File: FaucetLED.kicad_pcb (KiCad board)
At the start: 2 copper layers, 34.5 x 25.4 mm, 30 parts, among them P1 CONN_01X03, P2 CONN_01X02, P3 CONN_01X02, P4 CONN_01X03, P5 CONN_01X02, U1 TLV70033DDC, U2 STM32L052KxTx

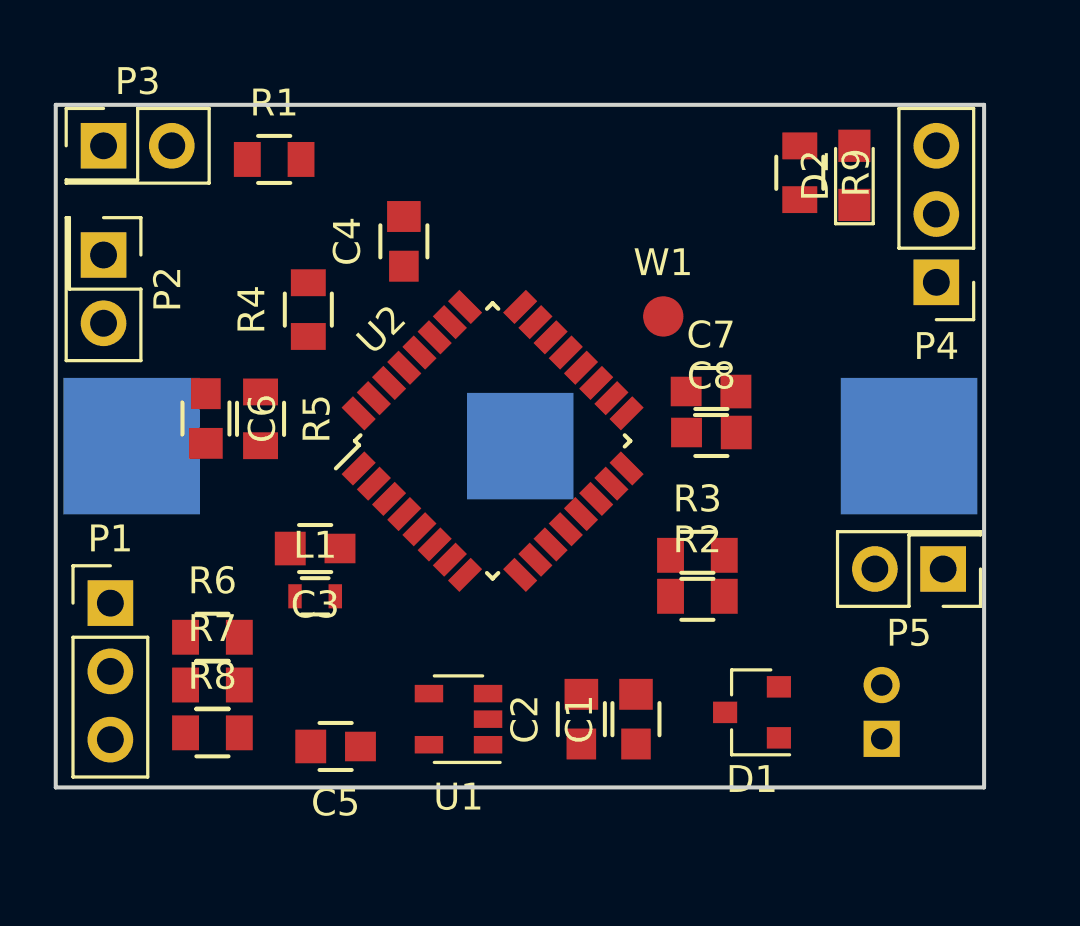
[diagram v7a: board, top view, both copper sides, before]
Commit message: Add mounting holes for CU-18420-B enclosure.
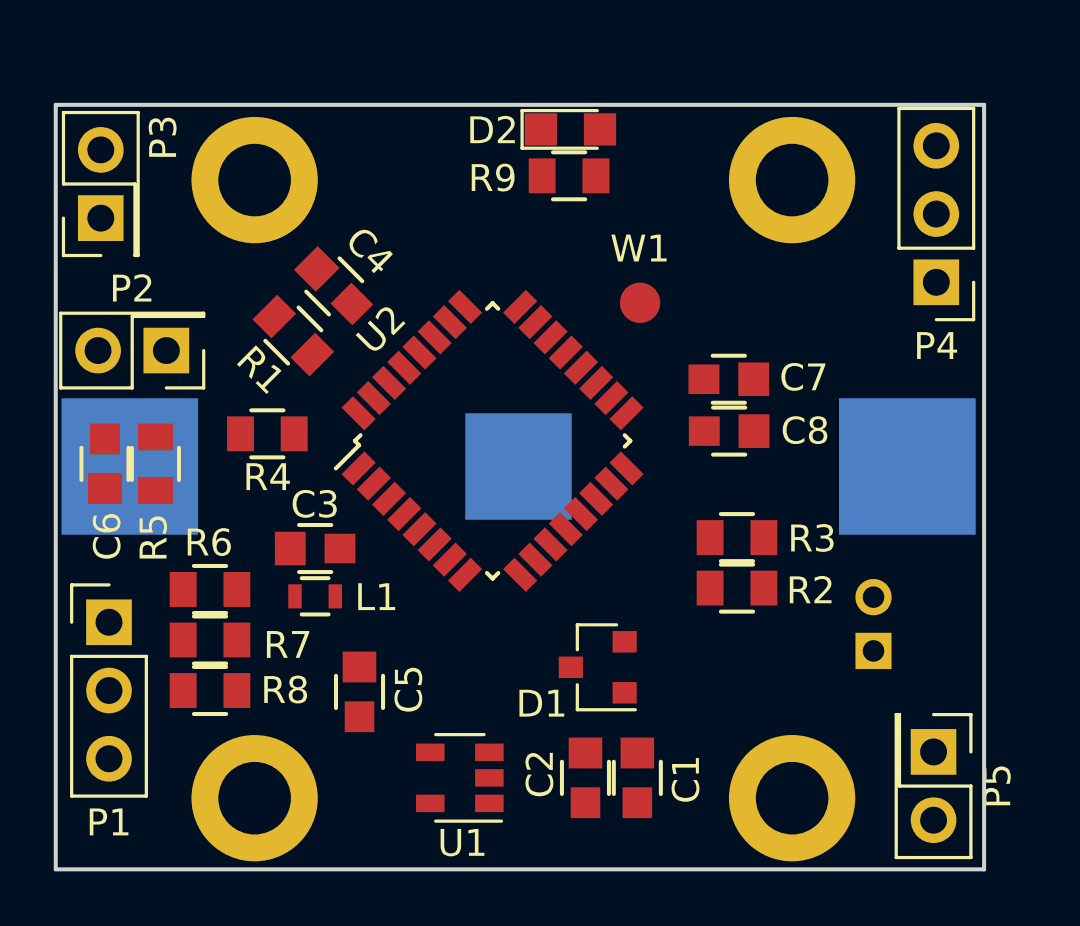
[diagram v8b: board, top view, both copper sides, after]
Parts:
- added REF**: MountingHole_2.7mm_M2.5_DIN965_Pad, Mounting_Holes:MountingHole_2.7mm_M2.5_DIN965_Pad, F.Cu at (109.0, 79.0)
- added REF**: MountingHole_2.7mm_M2.5_DIN965_Pad, Mounting_Holes:MountingHole_2.7mm_M2.5_DIN965_Pad, F.Cu at (129.0, 102.0)
- added REF**: MountingHole_2.7mm_M2.5_DIN965_Pad, Mounting_Holes:MountingHole_2.7mm_M2.5_DIN965_Pad, F.Cu at (129.0, 79.0)
- added REF**: MountingHole_2.7mm_M2.5_DIN965_Pad, Mounting_Holes:MountingHole_2.7mm_M2.5_DIN965_Pad, F.Cu at (109.0, 102.0)
- moved D2 10.7 mm to (120.8, 77.1), turned to 0 degrees
- moved R9 8.59 mm to (120.7, 78.8), turned to 180 degrees
- moved P5 6.82 mm to (134.3, 100.3), turned to 270 degrees
- moved R1 6.59 mm to (110.4, 84.8), turned to 315 degrees
- moved D1 5.98 mm to (121.8, 97.1)
- moved R4 4.87 mm to (109.5, 88.4), turned to 180 degrees
- moved R5 4.26 mm to (105.3, 89.6)
- moved P2 4.26 mm to (105.7, 85.3), turned to 180 degrees
- moved C6 4.12 mm to (103.4, 89.6)
- moved BT2 3.28 mm to (132.0, 96.5)
- moved C4 3.09 mm to (112.0, 83.0), turned to 135 degrees
- moved P3 2.69 mm to (103.3, 80.4), turned to 90 degrees
- moved C5 2.22 mm to (112.9, 98.0), turned to 90 degrees
- moved C2 2.19 mm to (121.3, 101.2)
- moved C1 2.18 mm to (123.2, 101.2)
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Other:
- board size 34.5 x 25.4 mm -> 34.5 x 28.4 mm
